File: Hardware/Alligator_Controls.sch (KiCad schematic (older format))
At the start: 25 parts, among them J1 Audio_In_L, J10 Feedback_CV, J11 Audio_In_R, J12 Audio_Out_R, J13 Audio_Out_L, J14 USB_B_Micro, J2 Delay_CV_L, J3 Conn_01x08_Female, J4 Conn_01x08_Female, J5 Conn_01x08_Female, J6 Conn_01x08_Female, J7 Mix_CV, J8 Delay_CV_R, J9 Clock

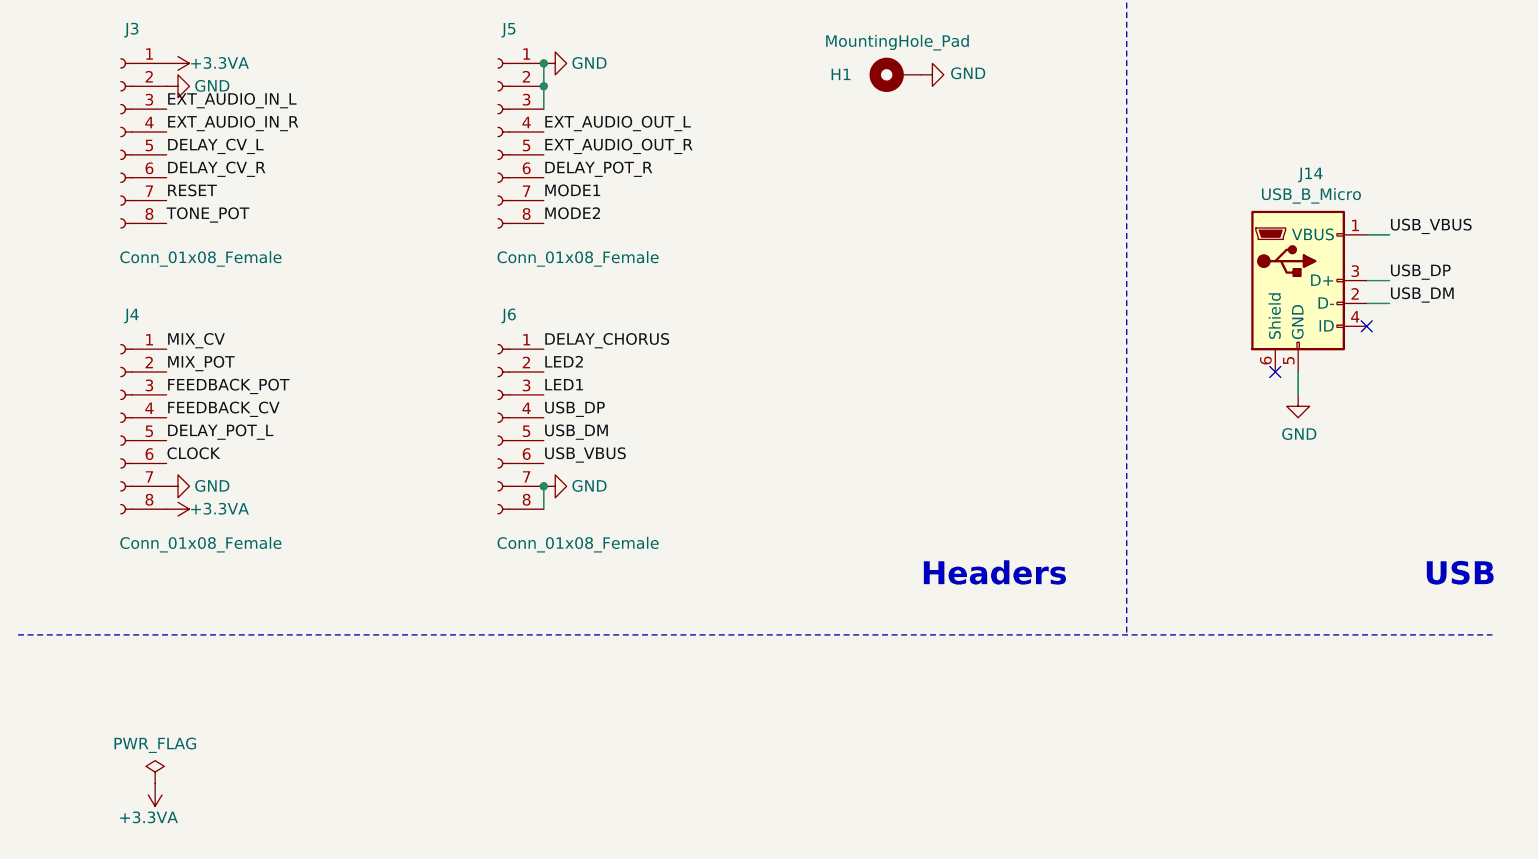
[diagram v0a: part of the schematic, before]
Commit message: Tooling holes added for SMT assembly; started routing control PCB
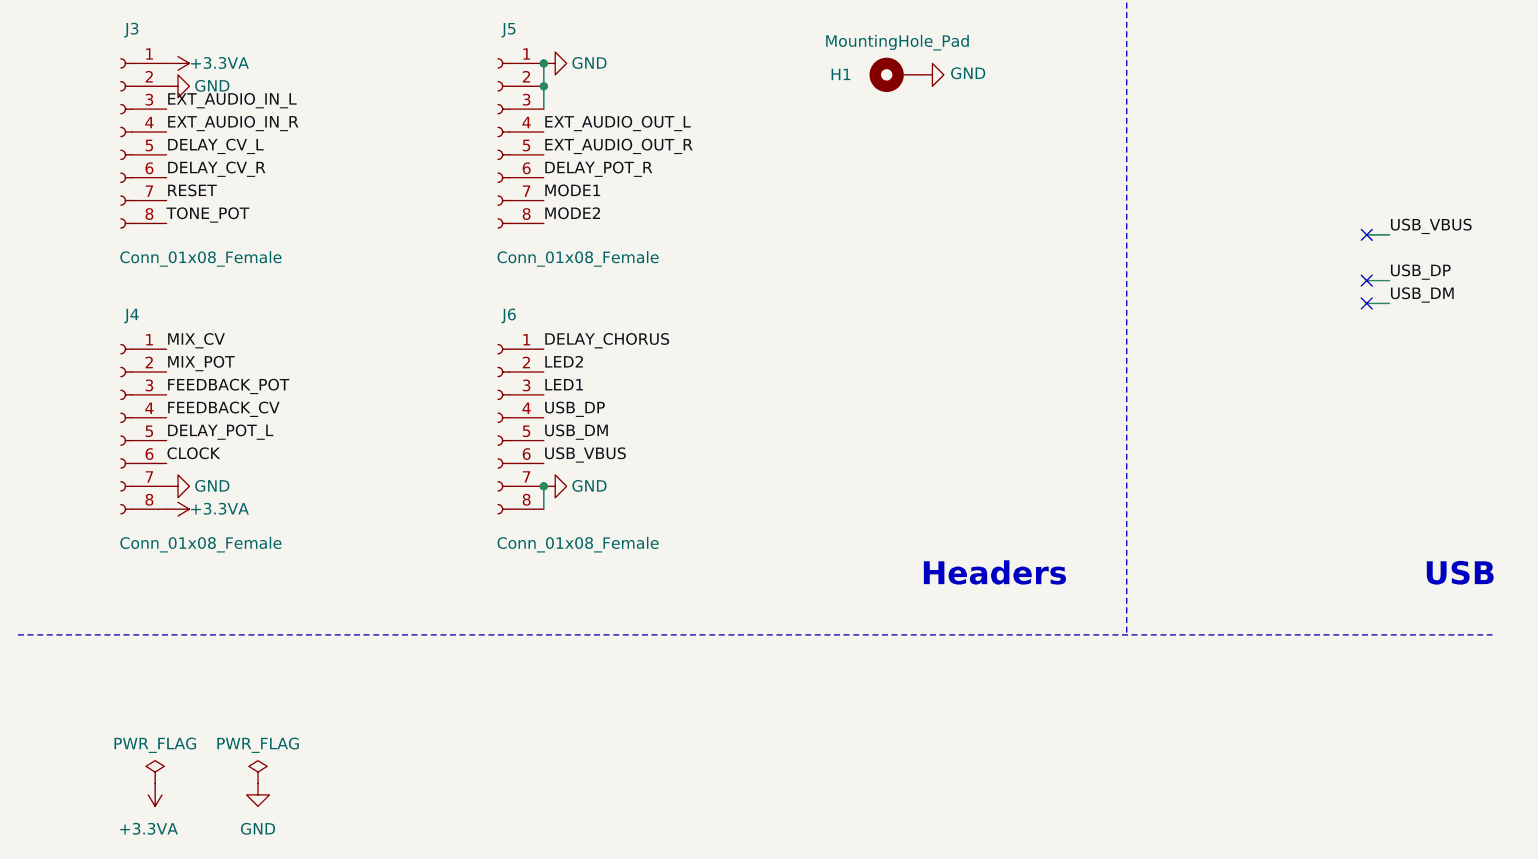
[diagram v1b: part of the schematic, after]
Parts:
- removed J14: USB_B_Micro, Connectors:USB_Micro-B, symbol Connector:USB_B_Micro
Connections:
- no-connect marks 4 -> 5
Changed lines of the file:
@@
 Text Label 4650 2000 0    50   ~ 0
 MIX_CV
-Text Label 6500 4750 0    50   ~ 0
-USB_VBUS
-Text Label 6500 5050 0    50   ~ 0
-USB_DM
-Text Label 6500 4950 0    50   ~ 0
-USB_DP
 Text Label 8050 2150 2    50   ~ 0
 LED1
@@
 Wire Wire Line
 	8450 2800 8550 2800
-$Comp
-L Connector:USB_B_Micro J14
-U 1 1 5F8CF76B
-P 6100 4950
-F 0 "J14" H 6157 5417 50  0000 C CNN
-F 1 "USB_B_Micro" H 6157 5326 50  0000 C CNN
-F 2 "Connectors:USB_Micro-B" H 6250 4900 50  0001 C CNN
-F 3 "~" H 6250 4900 50  0001 C CNN
-	1    6100 4950
-	1    0    0    -1
-$EndComp
-$Comp
-L power:GND #PWR027
-U 1 1 5F8CFC42
-P 6100 5450
-F 0 "#PWR027" H 6100 5200 50  0001 C CNN
-F 1 "GND" H 6105 5277 50  0000 C CNN
-F 2 "" H 6100 5450 50  0001 C CNN
-F 3 "" H 6100 5450 50  0001 C CNN
-	1    6100 5450
-	1    0    0    -1
-$EndComp
-Wire Wire Line
-	6100 5350 6100 5450
-NoConn ~ 6000 5350
-NoConn ~ 6400 5150
-Wire Wire Line
-	6400 4750 6500 4750
-Wire Wire Line
-	6400 4950 6500 4950
-Wire Wire Line
-	6400 5050 6500 5050
 Wire Notes Line
 	500  6500 6950 6500
@@
 Text Notes 9800 6350 0    100  ~ 20
 Potentiometers
-Text Notes 6650 6300 0    100  ~ 20
-USB
 Text Notes 9300 3350 0    100  ~ 20
 Switches and Buttons
@@
 Wire Notes Line
 	7200 500  7200 6500
-Wire Notes Line
-	5350 500  5350 6500
 $Comp
 L power:PWR_FLAG #FLG0101
@@
 P 1100 7150
 F 0 "#PWR0101" H 1100 7000 50  0001 C CNN
-F 1 "+3.3VA" H 1000 7300 50  0000 L CNN
+F 1 "+3.3VA" H 1000 7350 50  0000 L CNN
 F 2 "" H 1100 7150 50  0001 C CNN
 F 3 "" H 1100 7150 50  0001 C CNN
@@
 Text Label 10350 5550 0    50   ~ 0
 DELAY_POT_R
+Wire Notes Line
+	5350 500  5350 6500
+Text Notes 6650 6300 0    100  ~ 20
+USB
+Wire Wire Line
+	6400 5050 6500 5050
+Wire Wire Line
+	6400 4950 6500 4950
+Wire Wire Line
+	6400 4750 6500 4750
+Text Label 6500 4950 0    50   ~ 0
+USB_DP
+Text Label 6500 5050 0    50   ~ 0
+USB_DM
+Text Label 6500 4750 0    50   ~ 0
+USB_VBUS
+NoConn ~ 6400 4750
+NoConn ~ 6400 4950
+NoConn ~ 6400 5050
+$Comp
+L power:GND #PWR0102
+U 1 1 6025DB85
+P 1550 7150
+F 0 "#PWR0102" H 1550 6900 50  0001 C CNN
+F 1 "GND" H 1550 6950 50  0000 C CNN
+F 2 "" H 1550 7150 50  0001 C CNN
+F 3 "" H 1550 7150 50  0001 C CNN
+	1    1550 7150
+	1    0    0    -1
+$EndComp
+$Comp
+L power:PWR_FLAG #FLG0102
+U 1 1 6025E675
+P 1550 7150
+F 0 "#FLG0102" H 1550 7225 50  0001 C CNN
+F 1 "PWR_FLAG" H 1550 7323 50  0000 C CNN
+F 2 "" H 1550 7150 50  0001 C CNN
+F 3 "~" H 1550 7150 50  0001 C CNN
+	1    1550 7150
+	1    0    0    -1
+$EndComp
 $EndSCHEMATC

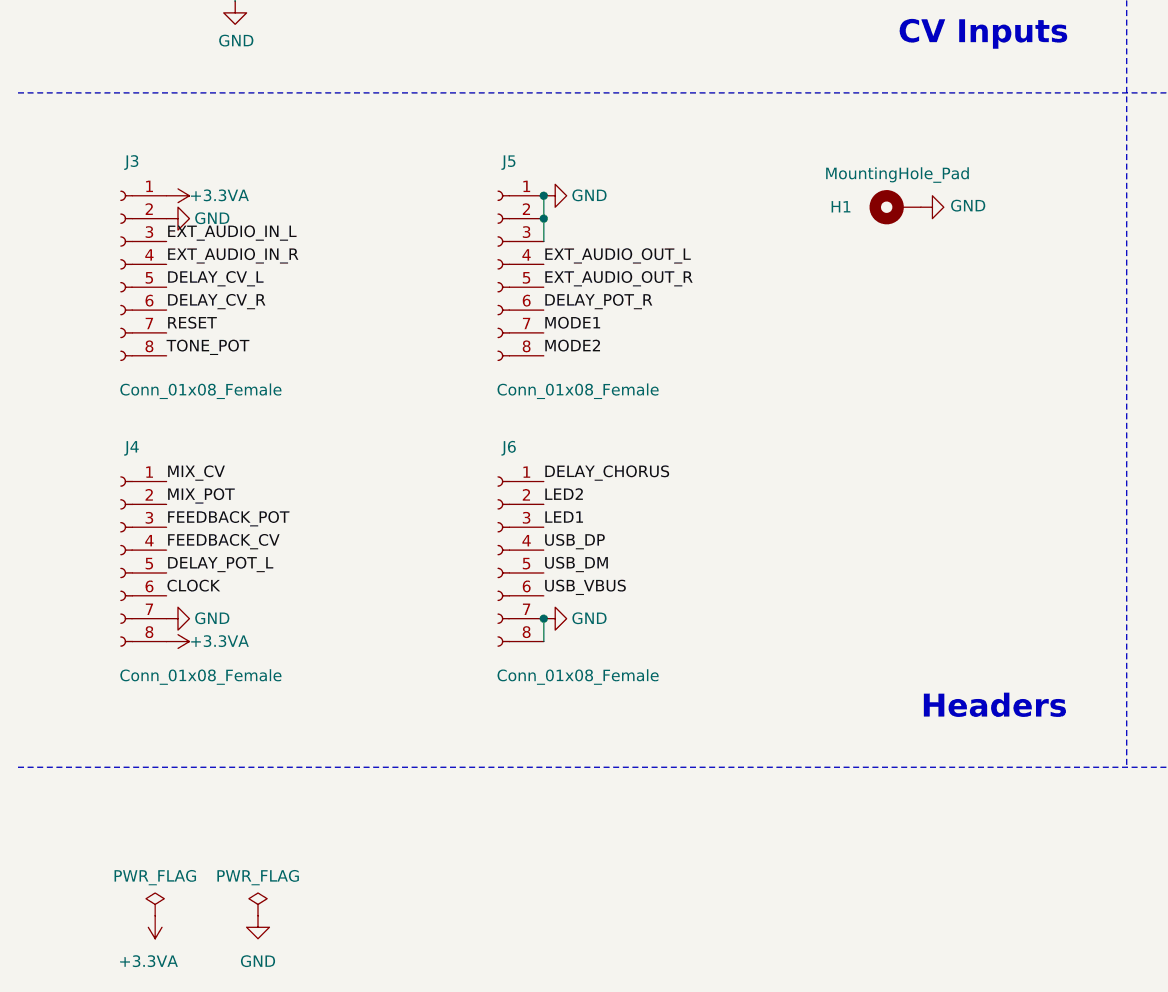
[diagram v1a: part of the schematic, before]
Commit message: Control PCB orientation tests
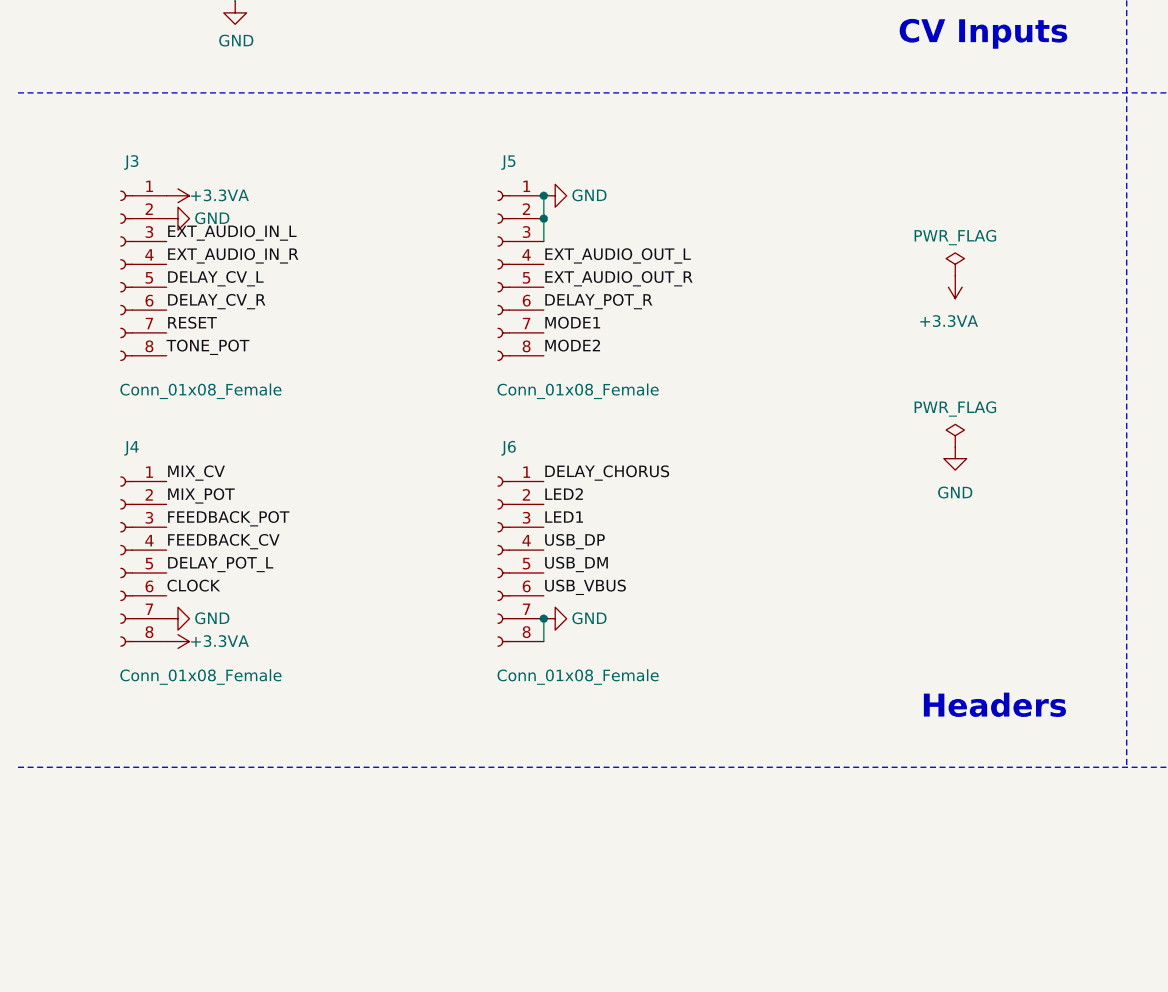
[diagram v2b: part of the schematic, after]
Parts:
- removed H1: MountingHole_Pad, Mounting_Holes:MountingHole_3.2mm_M3, symbol Mechanical:MountingHole_Pad
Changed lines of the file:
@@
 TONE_POT
-$Comp
-L Mechanical:MountingHole_Pad H1
-U 1 1 5FA61035
-P 4350 4050
-F 0 "H1" V 4350 4300 50  0000 C CNN
-F 1 "MountingHole_Pad" V 4496 4053 50  0000 C CNN
-F 2 "Mounting_Holes:MountingHole_3.2mm_M3" H 4350 4050 50  0001 C CNN
-F 3 "~" H 4350 4050 50  0001 C CNN
-	1    4350 4050
-	0    -1   -1   0
-$EndComp
-$Comp
-L power:GND #PWR017
-U 1 1 5FA62848
-P 4450 4050
-F 0 "#PWR017" H 4450 3800 50  0001 C CNN
-F 1 "GND" V 4455 3922 50  0000 R CNN
-F 2 "" H 4450 4050 50  0001 C CNN
-F 3 "" H 4450 4050 50  0001 C CNN
-	1    4450 4050
-	0    -1   -1   0
-$EndComp
 $Comp
 L Device:R_POT Tone_Pot1
@@
 L power:PWR_FLAG #FLG0101
 U 1 1 5F6CF78D
-P 1100 7150
-F 0 "#FLG0101" H 1100 7225 50  0001 C CNN
-F 1 "PWR_FLAG" H 1100 7323 50  0000 C CNN
-F 2 "" H 1100 7150 50  0001 C CNN
-F 3 "~" H 1100 7150 50  0001 C CNN
-	1    1100 7150
+P 4600 4350
+F 0 "#FLG0101" H 4600 4425 50  0001 C CNN
+F 1 "PWR_FLAG" H 4600 4523 50  0000 C CNN
+F 2 "" H 4600 4350 50  0001 C CNN
+F 3 "~" H 4600 4350 50  0001 C CNN
+	1    4600 4350
 	1    0    0    -1
 $EndComp
@@
 L power:+3.3VA #PWR0101
 U 1 1 5F6CFD38
-P 1100 7150
-F 0 "#PWR0101" H 1100 7000 50  0001 C CNN
-F 1 "+3.3VA" H 1000 7350 50  0000 L CNN
-F 2 "" H 1100 7150 50  0001 C CNN
-F 3 "" H 1100 7150 50  0001 C CNN
-	1    1100 7150
+P 4600 4350
+F 0 "#PWR0101" H 4600 4200 50  0001 C CNN
+F 1 "+3.3VA" H 4500 4550 50  0000 L CNN
+F 2 "" H 4600 4350 50  0001 C CNN
+F 3 "" H 4600 4350 50  0001 C CNN
+	1    4600 4350
 	-1   0    0    1
 $EndComp
@@
 L power:GND #PWR0102
 U 1 1 6025DB85
-P 1550 7150
-F 0 "#PWR0102" H 1550 6900 50  0001 C CNN
-F 1 "GND" H 1550 6950 50  0000 C CNN
-F 2 "" H 1550 7150 50  0001 C CNN
-F 3 "" H 1550 7150 50  0001 C CNN
-	1    1550 7150
+P 4600 5100
+F 0 "#PWR0102" H 4600 4850 50  0001 C CNN
+F 1 "GND" H 4600 4900 50  0000 C CNN
+F 2 "" H 4600 5100 50  0001 C CNN
+F 3 "" H 4600 5100 50  0001 C CNN
+	1    4600 5100
 	1    0    0    -1
 $EndComp
@@
 L power:PWR_FLAG #FLG0102
 U 1 1 6025E675
-P 1550 7150
-F 0 "#FLG0102" H 1550 7225 50  0001 C CNN
-F 1 "PWR_FLAG" H 1550 7323 50  0000 C CNN
-F 2 "" H 1550 7150 50  0001 C CNN
-F 3 "~" H 1550 7150 50  0001 C CNN
-	1    1550 7150
-	1    0    0    -1
-$EndComp
+P 4600 5100
+F 0 "#FLG0102" H 4600 5175 50  0001 C CNN
+F 1 "PWR_FLAG" H 4600 5273 50  0000 C CNN
+F 2 "" H 4600 5100 50  0001 C CNN
+F 3 "~" H 4600 5100 50  0001 C CNN
+	1    4600 5100
+	1    0    0    -1
+$EndComp
